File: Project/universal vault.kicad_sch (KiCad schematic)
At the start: 198 parts, among them J1 USB_C_Receptacle_USB2.0, SW1 RotaryEncoder_Switch, SW2 RotaryEncoder_Switch, SW4 SKQGABE010, U1 STM32F072CBUx, U2 XC6206PxxxMR, U5 74AHCT1G125

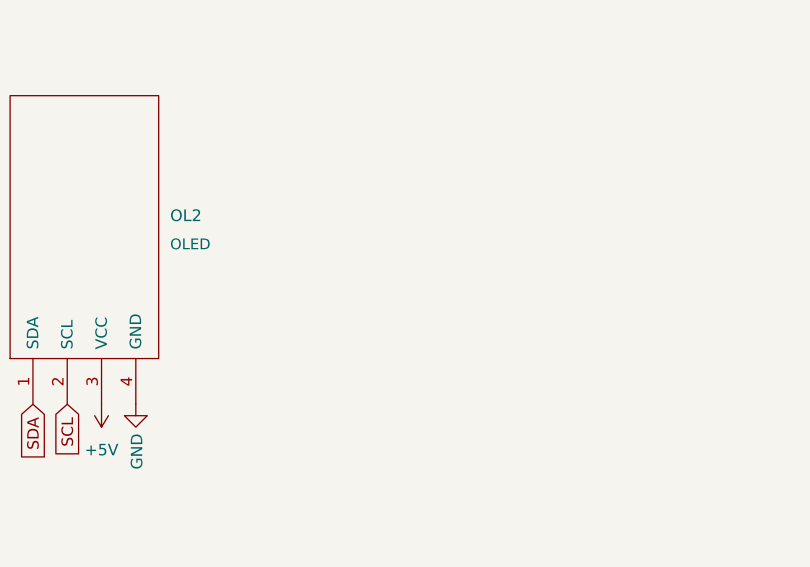
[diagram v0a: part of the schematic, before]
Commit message: added I2C pull up
added I2C pull up and updated production files
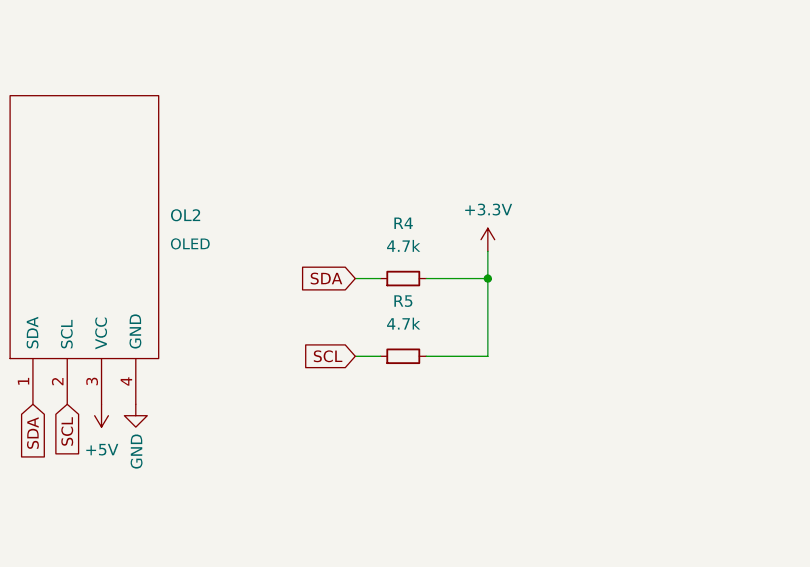
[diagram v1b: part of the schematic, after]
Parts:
- added R4, R5: 4.7k, Resistor_SMD:R_0402_1005Metric, symbol Device:R_Small
- C1, C11, C19, C2, C3, C4, C5, C7: LCSC (none) -> C1525; Package (none) -> 0402
- C10, C8: LCSC (none) -> C14445; Package (none) -> 0402
- C6: LCSC (none) -> C315248; Package (none) -> 0402
- D1: LCSC (none) -> C2827688; Package (none) -> SOT-143
- D_SPACE1, D_SPACE10, D_SPACE11, D_SPACE12, D_SPACE13, D_SPACE14, D_SPACE15, D_SPACE16, D_SPACE17, D_SPACE18, D_SPACE19, D_SPACE2, D_SPACE20, D_SPACE21, D_SPACE22, D_SPACE23, D_SPACE24, D_SPACE25, D_SPACE26, D_SPACE27, D_SPACE28, D_SPACE29, D_SPACE3, D_SPACE30, D_SPACE31, D_SPACE32, D_SPACE33, D_SPACE34, D_SPACE35, D_SPACE36, D_SPACE38, D_SPACE39, D_SPACE4, D_SPACE40, D_SPACE5, D_SPACE6, D_SPACE7, D_SPACE8, D_SPACE9: LCSC (none) -> C81598; Package (none) -> SOD-123
- F2: LCSC (none) -> C135341; Package (none) -> 1206
- J1: LCSC (none) -> C165948
- LED10, LED11, LED12, LED13, LED14, LED15, LED4, LED5, LED6, LED7, LED8, LED9: LCSC (none) -> C965555
- R1: LCSC (none) -> C25744; Package (none) -> 0402
- R2, R3: LCSC (none) -> C25905; Package (none) -> 0402
- SW4: LCSC (none) -> C115351
- U1: LCSC (none) -> C92504; Package (none) -> UFQFPN-48(7x7)
- U2: LCSC (none) -> C5446; Package (none) -> SOT-23
- U5: LCSC (none) -> C12494; Package (none) -> SOT-23
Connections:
- net +3V3: now also R4.2, R5.2
- net SCL: now also R5.1
- net SDA: now also R4.1

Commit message: small revision
added trackpad support, more bottom row support & 1 rotary
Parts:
- removed L1: 60R@100MHz, Inductor_SMD:L_1206_3216Metric, symbol Unified-Daughterboard-rescue:L_Core_Ferrite-Device
- added C9: 2.2uF, Capacitor_SMD:C_0805_2012Metric, symbol Device:C_Polarized
- added D_SPACE37, D_SPACE42: D, Diode_SMD:D_SOD-123F, symbol Device:D
- added K_SPACE35, K_SPACE36, K_SPACE39: KEYSW, PCM_marbastlib-mx:SW_MX_1u, symbol keyboard_parts:KEYSW
- added K_SPACE37, K_SPACE38: KEYSW, PCM_marbastlib-mx:SW_MX_1.5u, symbol keyboard_parts:KEYSW
- added SW3: RotaryEncoder_Switch, PCM_marbastlib-various:ROT_Alps_EC11E-Switch, symbol Device:RotaryEncoder_Switch
- added TP1: Conn_01x05_Pin, Connector_PinSocket_2.00mm:PinSocket_1x05_P2.00mm_Vertical, symbol Connector:Conn_01x05_Pin
- added UR6, UR7: 4.7k, Resistor_SMD:R_0805_2012Metric_Pad1.20x1.40mm_HandSolder, symbol device:R
- added UR8: 100k, Resistor_SMD:R_0805_2012Metric_Pad1.20x1.40mm_HandSolder, symbol device:R
- S1: value MX_stab -> ISO
- S2, S3: value MX_stab -> 2u
- S4: value MX_stab -> 2.25u
- S5: value MX_stab -> 2.75u
- S6, S7, S9: value MX_stab -> 3u
- S8: value MX_stab -> 6u
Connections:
- net +3V3: now also OL1.3 (VCC), OL2.3 (VCC), C9.1, TP1.2 (Pin_2), UR6.1, UR7.2
- net +5V: no longer OL1.3 (VCC), OL2.3 (VCC)
- net GND: now also SW3.C, TP1.3 (Pin_3), UR8.2
- net RGB MCU: now also U1.10 (PA0); no longer U1.31 (PA10)
- net col1: now also K_SPACE105.1, K_SPACE107.1, K_SPACE122.1
- net col2: now also K_SPACE106.1, K_SPACE111.1, K_SPACE117.1; no longer K_SPACE105.1, K_SPACE107.1, K_SPACE122.1
- net col3: now also K_SPACE114.1, K_SPACE120.1, K_SPACE124.1, K_SPACE128.1, K_SPACE37.1, K_SPACE39.1; no longer K_SPACE106.1, K_SPACE111.1, K_SPACE117.1
- net col4: now also K_SPACE35.1; no longer K_SPACE114.1, K_SPACE120.1, K_SPACE124.1, K_SPACE128.1
- net col5: now also K_SPACE110.1, K_SPACE36.1, SW3.S2
- net col6: now also K_SPACE38.1; no longer K_SPACE110.1
- net col7: no longer K_SPACE108.1, K_SPACE112.1, K_SPACE118.1
- net col8: now also K_SPACE108.1, K_SPACE112.1, K_SPACE118.1; no longer K_SPACE109.1, K_SPACE113.1, K_SPACE123.1
- net col9: now also K_SPACE109.1, K_SPACE113.1, K_SPACE123.1
- net rD: now also U1.26 (PB13); no longer U1.29 (PA8)
- net row1: now also U1.25 (PB12); no longer U1.26 (PB13)
- net row3: now also D_SPACE37.1 (K), D_SPACE42.1 (K)
- net at D_SPACE38.2 (A), K_SPACE115.2, K_SPACE116.2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: now also K_SPACE38.2; no longer K_SPACE110.2
- net at D_SPACE36.2 (A), K_SPACE114.2, K_SPACE120.2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: now also K_SPACE37.2, K_SPACE39.2
- net rE: now reaches U1.11 (PA1)
- net rE: now also SW3.A
- net rF: now reaches U1.12 (PA2)
- net rF: now also SW3.B
- net TP_clk: now reaches U1.30 (PA9)
- net TP_clk: now also TP1.1 (Pin_1), UR6.2
- new net: D_SPACE37.2 (A), K_SPACE35.2
- new net: D_SPACE42.2 (A), K_SPACE110.2, K_SPACE36.2, SW3.S1
- new net TP_RST: C9.2, TP1.5 (Pin_5), UR8.1
- new net TP_data: TP1.4 (Pin_4), U1.31 (PA10), UR7.1
- no-connect marks 14 -> 11
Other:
- note added: "1"
- note added: "125"
- note added: "150"
- note added: "175"
- note added: "2"
- note added: "225"
- note added: "275"
- note added: "3"
- note added: "6"
- note added: "Alpha"
- note added: "Capacitors"
- note added: "ESD Protection"
- note added: "ISO"
- note added: "Katana"
- note added: "Key Matrix"
- note added: "LEDS"
- note added: "NRST&BOOT"
- note added: "OLED"
- note added: "Ortho"
- note added: "RGB logic shifter"
- note added: "Trackpoint"
- note added: "USB"
- note added: "V,O,A,U,T"
- note added: "Vault"
- moved on the sheet: C1, C10, C11, C19, C2, C3, C4, C5, C6, C7, C8, D1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
